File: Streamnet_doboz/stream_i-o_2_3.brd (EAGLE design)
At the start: 193.1 x 71.6 mm, 241 parts, among them IC12 LD117AS33TR, IC3 BEM_VEDO, IC4 7805TV, J1 PIN1-2, Q1 20MHz, T1 BD242, T10 BD242, T11 BD242, T12 BD242, T13 BD242, T14 BD242, T15 BD242, T16 BD242, T17 BC858, T2 BD242, T3 BD242, T4 BD242, T5 BD242, T6 BD242, T7 BD242, T8 BD242, T9 BD242, U1 MAX232SOIC16, U2 PIC32MX250F128B-I_SS

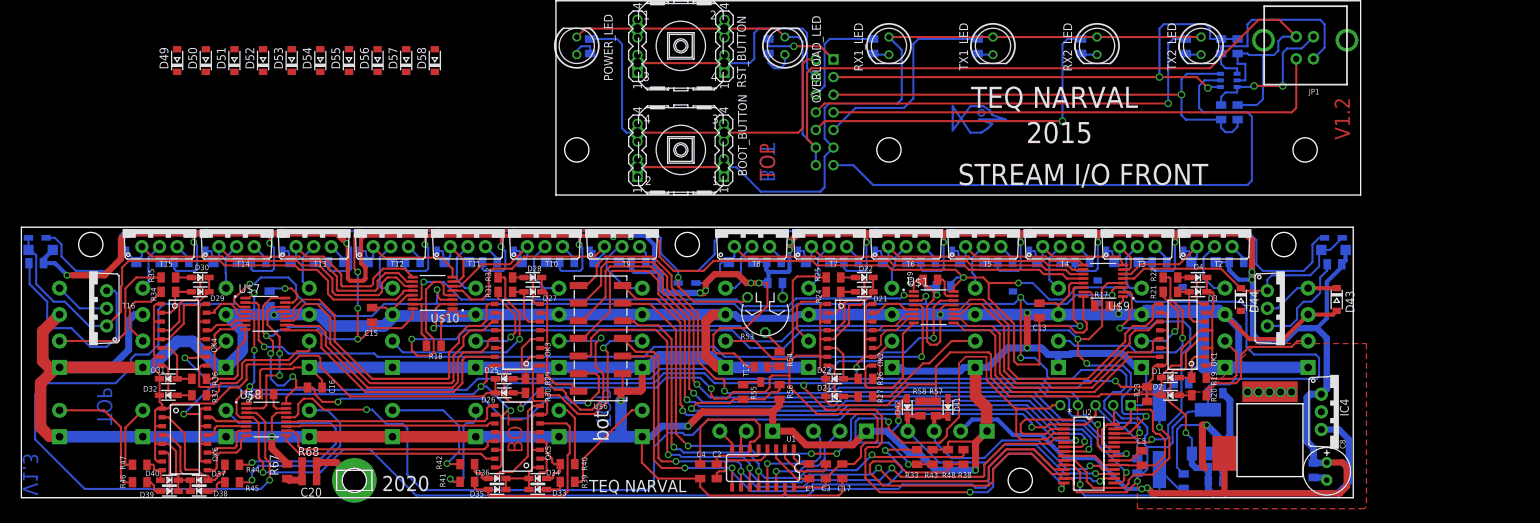
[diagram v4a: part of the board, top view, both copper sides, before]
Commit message: diodak felkerultek
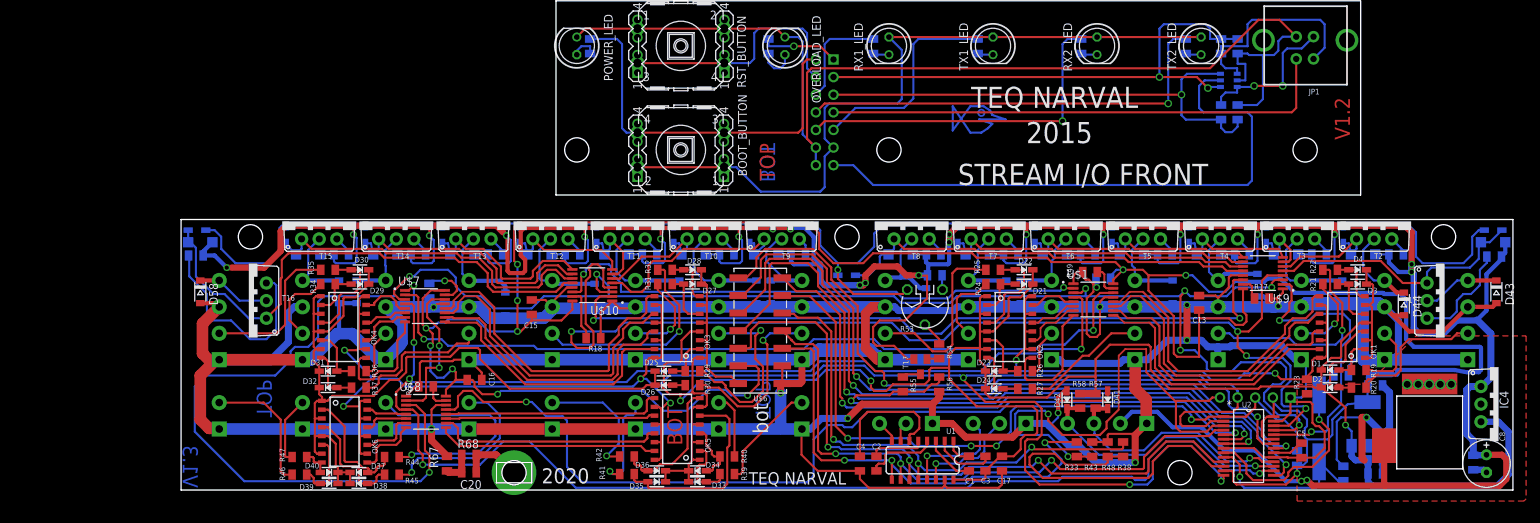
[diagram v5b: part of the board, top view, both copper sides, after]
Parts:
- moved D49 124.1 mm to (64.9, 32.5), flipped to the bottom, turned to 270 degrees
- moved D50 109.4 mm to (53.3, 31.4), flipped to the bottom, turned to 270 degrees
- moved D51 84.2 mm to (31.0, 32.5), flipped to the bottom, turned to 270 degrees
- moved D52 78.5 mm to (28.9, 32.5), flipped to the bottom, turned to 270 degrees
- moved D53 65.1 mm to (17.8, 32.5), flipped to the bottom, turned to 270 degrees
- moved D54 52.0 mm to (5.56, 32.1), flipped to the bottom, turned to 270 degrees
- moved D58 47.5 mm to (-51.3, 32.5), turned to 270 degrees
- moved D55 41.7 mm to (-7.30, 30.8), flipped to the bottom, turned to 270 degrees
- moved D57 34.7 mm to (-31.3, 32.5), flipped to the bottom, turned to 270 degrees
- moved D56 33.5 mm to (-28.7, 32.5), flipped to the bottom, turned to 270 degrees
- moved D44 23.5 mm to (122.2, 30.8)
- moved D47 23.1 mm to (88.9, 32.5)
- moved C8 23.0 mm to (134.1, 7.78)
- moved C9 23.0 mm to (132.2, 7.94)
- moved R17 23.0 mm to (101.8, 31.6)
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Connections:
- net +3V3: now also R23.2
- net +5V: no longer R23.2
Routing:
- net N$26: track 874.7 -> 914.1 mm
- net N$47: track 7.03 -> 13.5 mm
- net N$41: track 8.65 -> 15.0 mm
- net N$44: track 8.32 -> 14.6 mm
- net N$12: track 7.24 -> 13.3 mm
- net N$10: track 8.50 -> 14.4 mm
- net N$21: track 7.20 -> 12.7 mm
- net N$15: track 6.81 -> 12.3 mm
- net N$38: track 9.35 -> 14.8 mm
- net N$53: track 6.98 -> 12.3 mm
- net N$24: track 8.35 -> 12.9 mm
- net N$35: track 10.7 -> 15.2 mm
- net N$18: track 6.83 -> 11.3 mm
- net N$50: track 6.66 -> 10.9 mm
- net N$7: track 8.83 -> 12.3 mm
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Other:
- board size 193.1 x 71.6 mm -> 192 x 70.5 mm

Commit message: stream finish
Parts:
- moved D56 34.9 mm to (-63.7, 32.5)
- moved C8 34.6 mm to (99.5, 7.78)
- moved C9 34.6 mm to (97.6, 7.94)
- moved T1 34.6 mm to (93.5, 31.3)
- moved ZOLD_4P1 34.6 mm to (97.3, 28.5)
- moved C14 34.6 mm to (44.3, 34.4)
- moved D10 34.6 mm to (34.4, 40.8)
- moved D47 34.6 mm to (54.3, 32.5)
- moved D48 34.6 mm to (32.4, 32.5)
- moved D58 34.6 mm to (-85.9, 32.5)
- moved LED16 34.6 mm to (-85.9, 39.7)
- moved R49 34.6 mm to (42.4, 35.4)
- moved T16 34.6 mm to (-78.9, 31.3)
- moved C1 34.6 mm to (24.9, 7.78)
- moved C10 34.6 mm to (83.5, 6.35)
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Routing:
- net +3V3: track 389.5 -> 394.8 mm
- net N$168: track 55.1 -> 51.6 mm
- net N$166: track 5.61 -> 2.63 mm
- net N$164: track 165.4 -> 163.9 mm
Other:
- board size 192 x 70.5 mm -> 204.7 x 70.5 mm
- board text added: "2022"
- board text added: "STREAM I-O_1_4_SSOP"
- board text added: "V1.4"
- board text removed: "2015"
- board text removed: "2020"
- board text removed: "STREAM I/O"
- board text removed: "V1.2"
- board text removed: "V1.3"

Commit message: Streamnet finished
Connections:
- net CHECK: now also U$8.14; no longer U$8.13
- net N$26: now also U$8.13; no longer U$8.14
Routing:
- net CHECK: track 136.9 -> 136.3 mm
- net N$26: track 913.7 -> 913.2 mm
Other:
- board text added: "Kimeneti csog 1-8"
- board text added: "Kimeneti csog 8-16"
- board text added: "gomb 1-8"
- board text added: "opto 1-4"
- board text added: "opto 12-16"
- board text added: "opto 17-20"
- board text added: "opto 20-24"
- board text added: "opto 5-8"
- board text added: "opto 9-12"
- board text added: "uC SDI"
- board text added: "uC SDO"
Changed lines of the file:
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@@
 <circle x="61.3225" y="58.3475" radius="0.0254" width="0.254" layer="16"/>
 <text x="18.7325" y="80.01" size="1.778" layer="22">Elő 1.2: Az előlapi ledek fehér kontúrja jó irányban áll, de a ledek forognak!</text>
-<wire x1="53.0225" y1="22.70125" x2="53.18125" y2="22.5425" width="0.3048" layer="107"/>
+<text x="65.405" y="23.97125" size="1.016" layer="25" font="vector" ratio="15" distance="40">Kimeneti
+csog
+1-8</text>
+<text x="-33.3375" y="20.16125" size="1.016" layer="25" font="vector" ratio="15" distance="40">Kimeneti
+csog
+8-16</text>
+<text x="43.4975" y="25.7175" size="1.27" layer="25" font="vector" ratio="15" distance="40">gomb
+1-8</text>
+<text x="63.5" y="19.3675" size="1.27" layer="25" font="vector" ratio="15" distance="40">opto
+1-4</text>
+<wire x1="67.6275" y1="22.225" x2="70.1675" y2="24.765" width="0.4064" layer="25"/>
+<wire x1="70.1675" y1="24.765" x2="74.13625" y2="24.765" width="0.4064" layer="25"/>
+<wire x1="74.13625" y1="24.765" x2="73.66" y2="25.24125" width="0.4064" layer="25"/>
+<wire x1="74.13625" y1="24.765" x2="73.66" y2="24.28875" width="0.4064" layer="25"/>
+<text x="26.19375" y="16.03375" size="1.27" layer="25" font="vector" ratio="15" distance="40">opto 5-8</text>
+<text x="-25.87625" y="30.7975" size="1.27" layer="25" font="vector" ratio="15" distance="40" rot="R270">opto 9-12</text>
+<wire x1="-24.60625" y1="30.7975" x2="-24.60625" y2="31.59125" width="0.3048" layer="25"/>
+<wire x1="-24.60625" y1="31.59125" x2="-23.8125" y2="32.385" width="0.3048" layer="25"/>
+<wire x1="-23.8125" y1="32.385" x2="-22.38375" y2="32.385" width="0.3048" layer="25"/>
+<wire x1="-22.38375" y1="32.385" x2="-21.43125" y2="31.115" width="0.3048" layer="25"/>
+<wire x1="-21.43125" y1="31.115" x2="-21.43125" y2="31.59125" width="0.3048" layer="25"/>
+<wire x1="-21.43125" y1="31.115" x2="-21.9075" y2="31.27375" width="0.3048" layer="25"/>
+<text x="-32.385" y="7.62" size="1.27" layer="25" font="vector" ratio="15" distance="40" rot="R45">opto 17-20</text>
+<text x="-80.645" y="7.62" size="1.27" layer="25" font="vector" ratio="15" distance="40" rot="R45">opto 20-24</text>
+<text x="-80.48625" y="18.57375" size="1.27" layer="25" font="vector" ratio="15" distance="40" rot="R45">opto 12-16</text>
+<text x="69.5325" y="31.59125" size="0.8128" layer="25" font="vector" ratio="15" distance="40">uC SDO</text>
+<wire x1="71.12" y1="33.655" x2="71.4375" y2="33.3375" width="0.3048" layer="25"/>
+<wire x1="71.4375" y1="33.3375" x2="71.4375" y2="31.27375" width="0.3048" layer="25"/>
+<wire x1="71.4375" y1="31.27375" x2="69.69125" y2="31.27375" width="0.3048" layer="25"/>
+<wire x1="-49.53" y1="16.1925" x2="-48.73625" y2="16.1925" width="0.3048" layer="25"/>
+<wire x1="-48.73625" y1="16.1925" x2="-48.73625" y2="15.08125" width="0.3048" layer="25"/>
+<wire x1="-48.73625" y1="15.08125" x2="-44.60875" y2="15.08125" width="0.3048" layer="25"/>
+<wire x1="-49.53" y1="16.1925" x2="-49.2125" y2="16.51" width="0.3048" layer="25"/>
+<wire x1="-49.53" y1="16.1925" x2="-49.2125" y2="15.875" width="0.3048" layer="25"/>
+<text x="-44.29125" y="14.76375" size="0.8128" layer="25" font="vector" ratio="15" distance="40">uC SDI</text>
+<wire x1="71.12" y1="33.655" x2="71.4375" y2="33.655" width="0.3048" layer="25"/>
+<wire x1="71.12" y1="33.655" x2="71.12" y2="33.3375" width="0.3048" layer="25"/>
 </plain>
 <attributes>
@@
 </element>
 <element name="POWER_LED" library="led" package="LED5MM" value="KEK" x="2.87375" y="68.04875" smashed="yes" rot="R270">
-<attribute name="NAME" x="-2.30785" y="73.12875" size="1.27" layer="25" font="vector" ratio="25" rot="R270"/>
+<attribute name="NAME" x="7.21715" y="65.985" size="1.27" layer="25" font="vector" ratio="25" rot="R270"/>
 </element>
 <element name="OVERLOAD_LED" library="led" package="LED5MM" value="RED" x="32.88125" y="68.04875" smashed="yes" rot="R270">
-<attribute name="NAME" x="27.69965" y="76.30375" size="1.27" layer="25" font="vector" ratio="25" rot="R270"/>
+<attribute name="NAME" x="31.50965" y="64.55625" size="1.27" layer="25" font="vector" ratio="25" rot="R270"/>
 </element>
 <element name="RX1_LED" library="led" package="LED5MM" value="ORANGE" x="48" y="68" smashed="yes" rot="R270">
@@
 </element>
 <element name="U$1" library="SCT2167" package="SSOP" value="SCT2167SSOP" x="42.8625" y="31.4325" smashed="yes">
-<attribute name="NAME" x="38.84875" y="26.8125" size="1.27" layer="25"/>
+<attribute name="NAME" x="38.84875" y="26.8125" size="1.27" layer="25" font="vector" ratio="15"/>
 </element>
 <element name="U$7" library="SCT2167" package="SSOP" value="SCT2167SSOP" x="-53.49875" y="30.48" smashed="yes">
-<attribute name="NAME" x="-54.49625" y="33.95625" size="1.27" layer="25"/>
+<attribute name="NAME" x="-54.49625" y="33.95625" size="1.27" layer="25" font="vector" ratio="15"/>
 </element>
 <element name="U$8" library="SCT2167" package="SSOP" value="SCT2167SSOP" x="-53.34" y="15.24" smashed="yes">
-<attribute name="NAME" x="-55.13125" y="20.145" size="1.27" layer="25"/>
+<attribute name="NAME" x="-55.13125" y="20.145" size="1.27" layer="25" font="vector" ratio="15"/>
 </element>
 <element name="U$9" library="SCT2167" package="SSOP" value="SCT2167SSOP" x="67.31" y="35.2425" smashed="yes" rot="R180">
-<attribute name="NAME" x="68.625" y="29.54375" size="1.27" layer="25" rot="R180"/>
+<attribute name="NAME" x="68.625" y="29.54375" size="1.27" layer="25" font="vector" ratio="15" rot="R180"/>
 </element>
 <element name="U$10" library="SCT2167" package="SSOP" value="SCT2167SSOP" x="-29.36875" y="33.49625" smashed="yes" rot="R180">
-<attribute name="NAME" x="-27.41875" y="30.49625" size="1.27" layer="25" rot="R180"/>
+<attribute name="NAME" x="-27.41875" y="30.49625" size="1.27" layer="25" font="vector" ratio="15" rot="R180"/>
 </element>
 <element name="D43" library="dp_devices" package="SOD-123" value="" x="100.965" y="32.54375" smashed="yes" rot="R270">
@@
 <wire x1="4.60375" y1="13.335" x2="2.54" y2="11.27125" width="0.3048" layer="16"/>
 <wire x1="2.54" y1="11.27125" x2="2.54" y2="6.0325" width="0.3048" layer="16"/>
-<contactref element="U$8" pad="13"/>
-<wire x1="-50.47" y1="15.565" x2="-49.205" y2="15.565" width="0.3048" layer="1"/>
-<wire x1="-49.205" y1="15.565" x2="-48.73625" y2="16.03375" width="0.3048" layer="1"/>
-<wire x1="-48.73625" y1="16.03375" x2="-48.73625" y2="17.4625" width="0.3048" layer="1"/>
-<wire x1="-48.73625" y1="17.4625" x2="-47.9425" y2="18.25625" width="0.3048" layer="1"/>
+<wire x1="-48.895" y1="17.30375" x2="-47.9425" y2="18.25625" width="0.3048" layer="1"/>
+<contactref element="U$8" pad="14"/>
+<wire x1="-48.895" y1="17.30375" x2="-48.895" y2="16.51" width="0.3048" layer="1"/>
+<wire x1="-48.895" y1="16.51" x2="-49.2125" y2="16.1925" width="0.3048" layer="1"/>
+<wire x1="-49.2125" y1="16.1925" x2="-50.4475" y2="16.1925" width="0.3048" layer="1"/>
+<wire x1="-50.4475" y1="16.1925" x2="-50.47" y2="16.215" width="0.3048" layer="1"/>
 </signal>
 <signal name="POWER">
@@
 <contactref element="U$8" pad="1"/>
 <contactref element="R51" pad="2"/>
-<contactref element="U$8" pad="14"/>
 <contactref element="U$9" pad="1"/>
 <contactref element="R17" pad="2"/>
@@
 <wire x1="-54.39" y1="18.89125" x2="-54.83375" y2="18.89125" width="0.3048" layer="1"/>
 <wire x1="-54.83375" y1="18.89125" x2="-56.21" y2="17.515" width="0.3048" layer="1"/>
-<wire x1="-50.47" y1="16.215" x2="-51.88875" y2="16.215" width="0.3048" layer="1"/>
-<wire x1="-51.88875" y1="16.215" x2="-52.54625" y2="15.5575" width="0.3048" layer="1"/>
-<wire x1="-52.54625" y1="15.5575" x2="-52.54625" y2="12.76375" width="0.3048" layer="1"/>
+<wire x1="-52.54625" y1="15.08125" x2="-52.54625" y2="12.76375" width="0.3048" layer="1"/>
 <wire x1="-32.23875" y1="33.17125" x2="-33.0275" y2="33.17125" width="0.3048" layer="1"/>
 <wire x1="-33.0275" y1="33.17125" x2="-35.08375" y2="31.115" width="0.3048" layer="1"/>
@@
 <wire x1="87.63" y1="29.1625" x2="86.0575" y2="29.1625" width="0.6096" layer="1"/>
 <wire x1="86.0575" y1="29.1625" x2="84.84625" y2="30.37375" width="0.6096" layer="1"/>
+<contactref element="U$8" pad="13"/>
+<wire x1="-50.47" y1="15.565" x2="-52.0625" y2="15.565" width="0.3048" layer="1"/>
+<wire x1="-52.0625" y1="15.565" x2="-52.54625" y2="15.08125" width="0.3048" layer="1"/>
 </signal>
 </signals>
@@
 </board>
 </drawing>
+<compatibility>
+<note version="6.3" minversion="6.2.2" severity="warning">
+Since Version 6.2.2 text objects can contain more than one line,
+which will not be processed correctly with this version.
+</note>
+</compatibility>
 </eagle>
